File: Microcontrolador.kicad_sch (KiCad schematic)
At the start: 3 parts

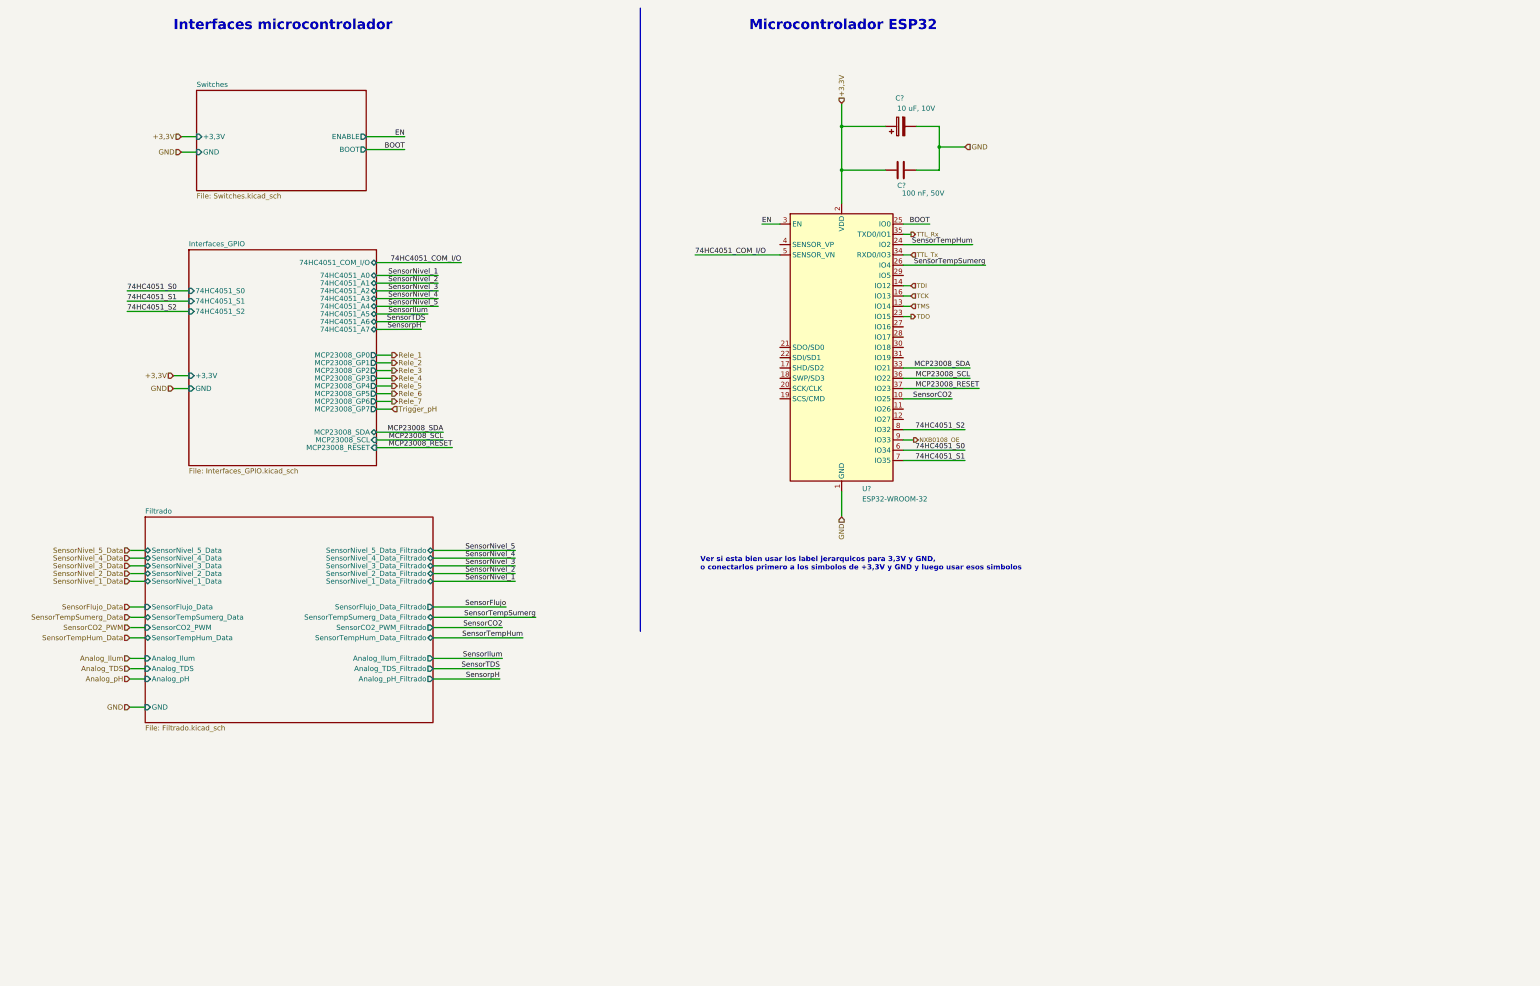
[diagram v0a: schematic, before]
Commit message: Ajuste del esquematico
Se cambio el integrado ESP32 por 2 tiras de pines de 1x15, se quitaron los switches EN y BOOT que ya estan en el NodeMCU, se quito el mutliplexor 74HC y se cablearon las I/O
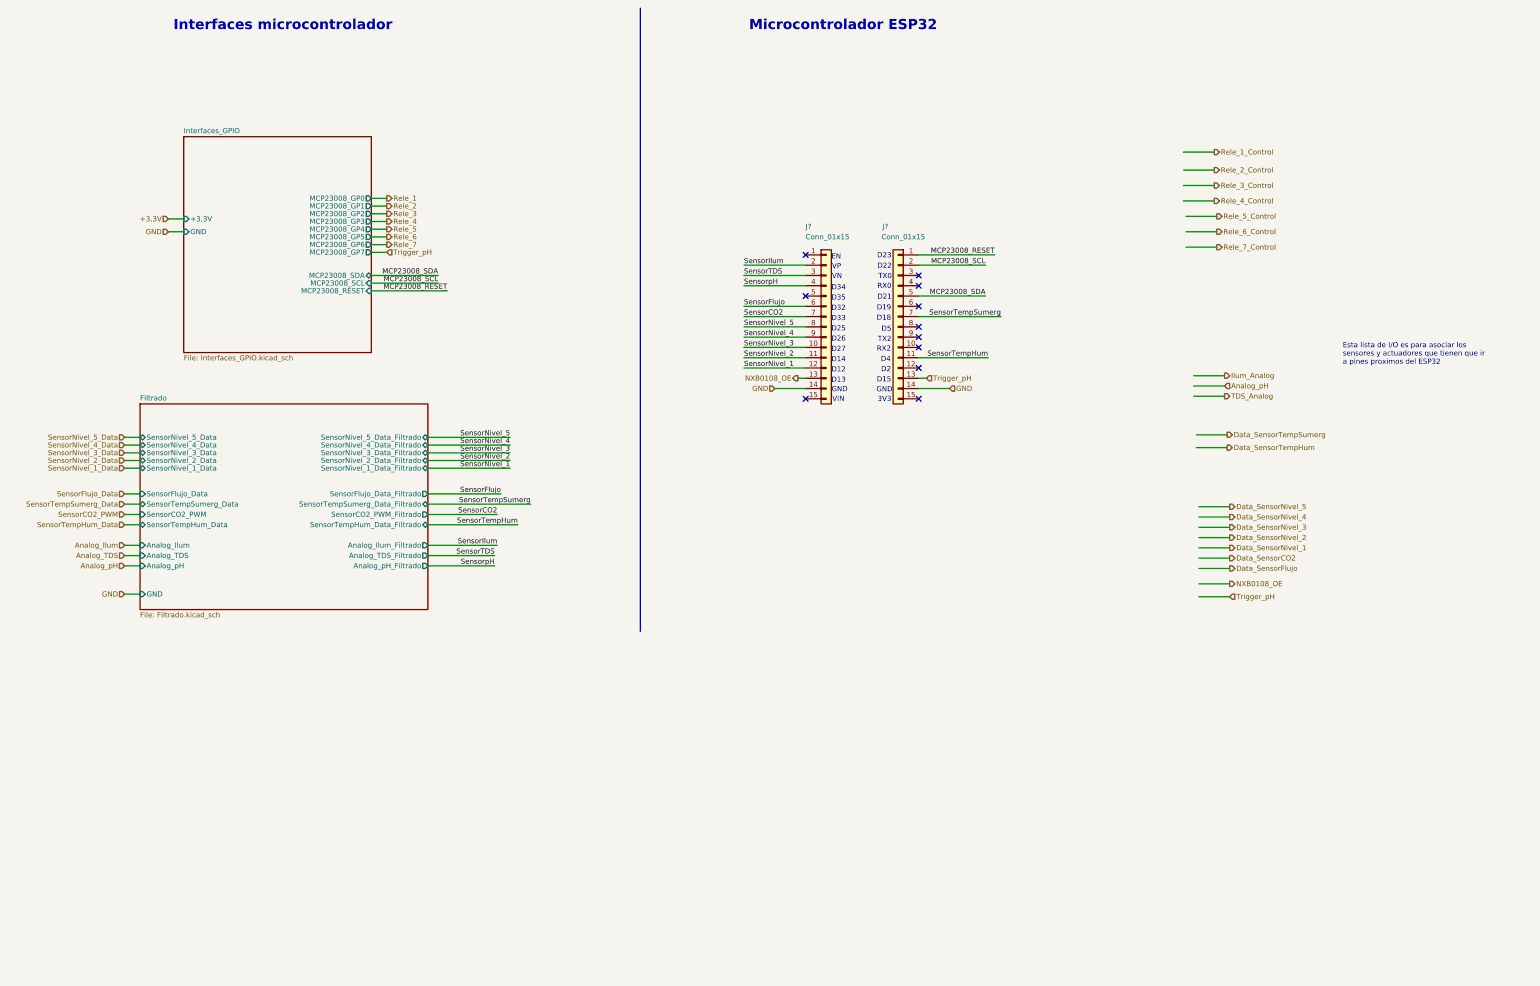
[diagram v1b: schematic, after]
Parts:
- removed C?: 100 nF, 50V, symbol Device:C
- removed C?: 10 uF, 10V, symbol Device:C_Polarized
- removed U?: ESP32-WROOM-32, RF_Module:ESP32-WROOM-32, symbol RF_Module:ESP32-WROOM-32
- added J?: Conn_01x15, symbol Connector_Generic:Conn_01x15
- added J?: Conn_01x15, Connector_JST:JST_SUR_SM08B-SURS-TF_1x08-1MP_P0.80mm_Horizontal, symbol Connector_Generic:Conn_01x15
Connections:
- net GND: now also J?.14 (Pin_14), J?.14 (Pin_14)
- net MCP23008_RESET: now also J?.1 (Pin_1)
- net MCP23008_SCL: now also J?.2 (Pin_2)
- net MCP23008_SDA: now also J?.5 (Pin_5)
- net NXB0108_OE: now also J?.13 (Pin_13)
- net SensorCO2: now also J?.7 (Pin_7)
- net SensorFlujo: now also J?.6 (Pin_6)
- net SensorIlum: now also J?.2 (Pin_2)
- net SensorNivel_1: now also J?.12 (Pin_12)
- net SensorNivel_2: now also J?.11 (Pin_11)
- net SensorNivel_3: now also J?.10 (Pin_10)
- net SensorNivel_4: now also J?.9 (Pin_9)
- net SensorNivel_5: now also J?.8 (Pin_8)
- net SensorTDS: now also J?.3 (Pin_3)
- net SensorTempHum: now also J?.11 (Pin_11)
- net SensorTempSumerg: now also J?.7 (Pin_7)
- net SensorpH: now also J?.4 (Pin_4)
- net Trigger_pH: now also J?.13 (Pin_13)
- no-connect marks 0 -> 11
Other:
- removed sheet Switches
- sheet Interfaces_GPIO ports: added none; removed 74HC4051_A0, 74HC4051_A1, 74HC4051_A2, 74HC4051_A3, 74HC4051_A4, 74HC4051_A5, 74HC4051_A6, 74HC4051_A7, 74HC4051_COM_I/O, 74HC4051_S0, 74HC4051_S1, 74HC4051_S2
- note added: "3V3"
- note added: "D12"
- note added: "D13"
- note added: "D14"
- note added: "D15"
- note added: "D18"
- note added: "D19"
- note added: "D2"
- note added: "D21"
- note added: "D22"
- note added: "D23"
- note added: "D25"
- note added: "D26"
- note added: "D27"
- note added: "D32"
- note added: "D33"
- note added: "D34"
- note added: "D35"
- note added: "D4"
- note added: "D5"
- note added: "EN"
- note added: "Esta lista de I/O es para asociar los sensores y actuadores que tienen que ir a pines proximos del ESP32"
- note added: "GND"
- note added: "RX0"
- note added: "RX2"
- note added: "TX0"
- note added: "TX2"
- note added: "VIN"
- note added: "VN"
- note added: "VP"
- note removed: "Ver si esta bien usar los label jerarquicos para 3,3V y GND, o conectarlos primero a los simbolos de +3,3V y GND y luego usar esos simbolos"

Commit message: Modificación de posición de circ. filtrado y circ. de adaptación de tensión
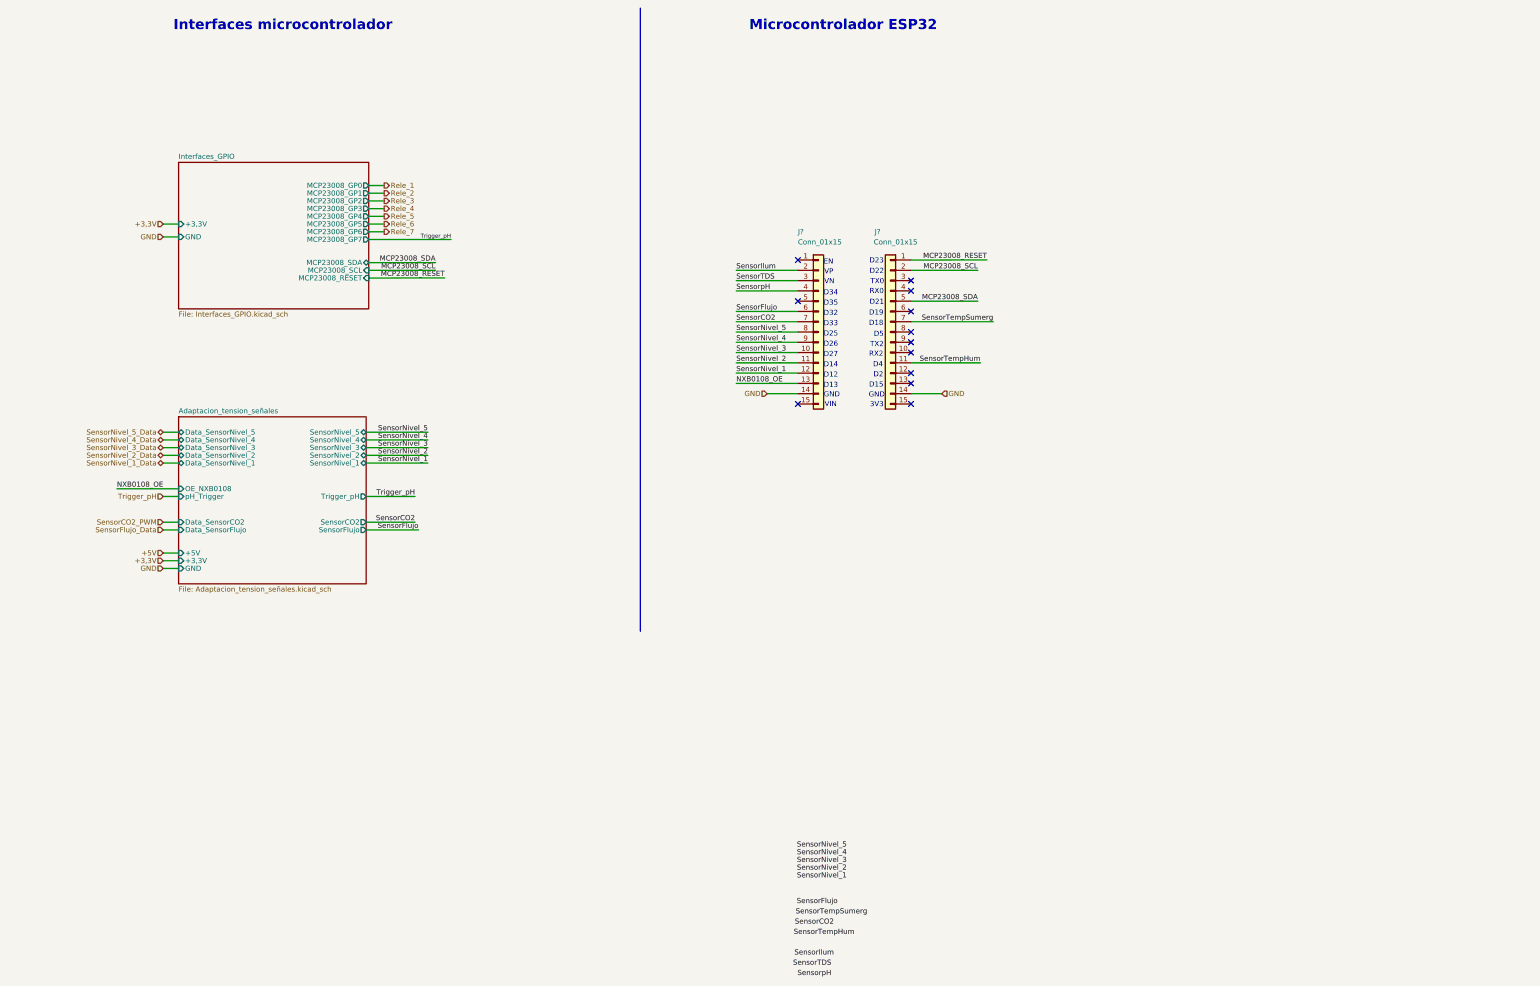
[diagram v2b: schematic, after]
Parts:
- removed J?: Conn_01x15, symbol Connector_Generic:Conn_01x15
- removed J?: Conn_01x15, Connector_JST:JST_SUR_SM08B-SURS-TF_1x08-1MP_P0.80mm_Horizontal, symbol Connector_Generic:Conn_01x15
- added J? (x2): Conn_01x15, Connector_JST:JST_SUR_SM08B-SURS-TF_1x08-1MP_P0.80mm_Horizontal, symbol Connector_Generic:Conn_01x15
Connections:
- net GND: now also J?.14 (Pin_14), J?.14 (Pin_14)
- net MCP23008_RESET: now also J?.1 (Pin_1)
- net MCP23008_SCL: now also J?.2 (Pin_2)
- net MCP23008_SDA: now also J?.5 (Pin_5)
- net NXB0108_OE: now also J?.13 (Pin_13)
- net SensorCO2: now also J?.7 (Pin_7)
- net SensorFlujo: now also J?.6 (Pin_6)
- net SensorIlum: now also J?.2 (Pin_2)
- net SensorNivel_1: now also J?.12 (Pin_12)
- net SensorNivel_2: now also J?.11 (Pin_11)
- net SensorNivel_3: now also J?.10 (Pin_10)
- net SensorNivel_4: now also J?.9 (Pin_9)
- net SensorNivel_5: now also J?.8 (Pin_8)
- net SensorTDS: now also J?.3 (Pin_3)
- net SensorTempHum: now also J?.11 (Pin_11)
- net SensorTempSumerg: now also J?.7 (Pin_7)
- net SensorpH: now also J?.4 (Pin_4)
- no-connect marks 11 -> 12
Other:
- removed sheet Filtrado
- added sheet Adaptacion_tension_señales (Adaptacion_tension_señales.kicad_sch)
- note removed: "Esta lista de I/O es para asociar los sensores y actuadores que tienen que ir a pines proximos del ESP32"

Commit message: Corrección de errores menores de esquematico
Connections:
- net SensorIlum: no longer J?.2 (Pin_2)
- net SensorTDS: no longer J?.3 (Pin_3)
- net SensorTempHum: no longer J?.11 (Pin_11)
- net SensorTempSumerg: no longer J?.7 (Pin_7)
- net SensorpH: no longer J?.4 (Pin_4)
- new net Analog_Ilum: J?.2 (Pin_2)
- new net Analog_TDS: J?.3 (Pin_3)
- new net Analog_pH: J?.4 (Pin_4)
- new net SensorTempHum_Data: J?.11 (Pin_11)
- new net SensorTempSumerg_Data: J?.7 (Pin_7)
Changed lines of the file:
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@@
+    (stroke (width 0) (type default) (color 0 0 0 0))
+  )
+  (wire (pts (xy 212.09 81.915) (xy 215.9 81.915))
     (stroke (width 0) (type default) (color 0 0 0 0))
   )
@@
     (stroke (width 0) (type default) (color 0 0 0 0))
   )
+  (wire (pts (xy 212.09 79.375) (xy 215.9 79.375))
+    (stroke (width 0) (type default) (color 0 0 0 0))
+  )
   (wire (pts (xy 109.855 69.215) (xy 130.175 69.215))
     (stroke (width 0) (type default) (color 0 0 0 0))
@@
     (stroke (width 0) (type default) (color 0 0 0 0))
   )
-  (wire (pts (xy 243.84 99.695) (xy 260.985 99.695))
-    (stroke (width 0) (type default) (color 0 0 0 0))
-  )
   (wire (pts (xy 109.22 118.745) (xy 124.46 118.745))
     (stroke (width 0) (type default) (color 0 0 0 0))
@@
     (stroke (width 0) (type default) (color 0 0 0 0))
   )
+  (wire (pts (xy 247.65 99.695) (xy 243.84 99.695))
+    (stroke (width 0) (type default) (color 0 0 0 0))
+  )
   (wire (pts (xy 59.055 146.685) (xy 62.865 146.685))
     (stroke (width 0) (type default) (color 0 0 0 0))
@@
     (stroke (width 0) (type default) (color 0 0 0 0))
   )
+  (wire (pts (xy 212.09 76.835) (xy 215.9 76.835))
+    (stroke (width 0) (type default) (color 0 0 0 0))
+  )
   (wire (pts (xy 113.665 67.31) (xy 109.855 67.31))
     (stroke (width 0) (type default) (color 0 0 0 0))
@@
     (stroke (width 0) (type default) (color 0 0 0 0))
   )
-  (wire (pts (xy 200.66 79.375) (xy 215.9 79.375))
-    (stroke (width 0) (type default) (color 0 0 0 0))
-  )
   (wire (pts (xy 59.055 122.555) (xy 62.865 122.555))
     (stroke (width 0) (type default) (color 0 0 0 0))
@@
     (stroke (width 0) (type default) (color 0 0 0 0))
   )
-  (wire (pts (xy 243.84 89.535) (xy 264.16 89.535))
-    (stroke (width 0) (type default) (color 0 0 0 0))
-  )
   (wire (pts (xy 59.055 68.58) (xy 62.865 68.58))
     (stroke (width 0) (type default) (color 0 0 0 0))
@@
     (stroke (width 0) (type default) (color 0 0 0 0))
   )
-  (wire (pts (xy 200.66 76.835) (xy 215.9 76.835))
+  (wire (pts (xy 247.65 89.535) (xy 243.84 89.535))
     (stroke (width 0) (type default) (color 0 0 0 0))
   )
@@
   )
   (wire (pts (xy 215.9 99.695) (xy 200.66 99.695))
-    (stroke (width 0) (type default) (color 0 0 0 0))
-  )
-  (wire (pts (xy 200.66 81.915) (xy 215.9 81.915))
     (stroke (width 0) (type default) (color 0 0 0 0))
   )
@@
     (effects (font (size 1.27 1.27)) (justify right bottom))
   )
-  (label "SensorTempSumerg" (at 264.16 89.535 180)
-    (effects (font (size 1.27 1.27)) (justify right bottom))
-  )
   (label "SensorNivel_2" (at 200.66 99.695 0)
     (effects (font (size 1.27 1.27)) (justify left bottom))
@@
     (effects (font (size 1.27 1.27)) (justify right bottom))
   )
-  (label "SensorTempHum" (at 260.985 99.695 180)
-    (effects (font (size 1.27 1.27)) (justify right bottom))
-  )
   (label "SensorFlujo" (at 200.66 86.995 0)
     (effects (font (size 1.27 1.27)) (justify left bottom))
@@
   )
   (label "NXB0108_OE" (at 200.66 104.775 0)
-    (effects (font (size 1.27 1.27)) (justify left bottom))
-  )
-  (label "SensorpH" (at 200.66 81.915 0)
-    (effects (font (size 1.27 1.27)) (justify left bottom))
-  )
-  (label "SensorTDS" (at 200.66 79.375 0)
     (effects (font (size 1.27 1.27)) (justify left bottom))
   )
@@
     (effects (font (size 1.27 1.27)) (justify left bottom))
   )
-  (label "SensorIlum" (at 200.66 76.835 0)
-    (effects (font (size 1.27 1.27)) (justify left bottom))
-  )
   (label "SensorCO2" (at 224.79 238.76 180)
     (effects (font (size 1.27 1.27)) (justify right bottom))
@@
     (effects (font (size 1.27 1.27)) (justify right bottom))
   )
+  (hierarchical_label "SensorTempHum_Data" (shape bidirectional) (at 247.65 99.695 0)
+    (effects (font (size 1.27 1.27)) (justify left))
+  )
   (hierarchical_label "+5V" (shape input) (at 59.055 146.685 180)
     (effects (font (size 1.27 1.27)) (justify right))
@@
     (effects (font (size 1.27 1.27)) (justify right))
   )
+  (hierarchical_label "Analog_TDS" (shape input) (at 212.09 79.375 180)
+    (effects (font (size 1.27 1.27)) (justify right))
+  )
   (hierarchical_label "GND" (shape input) (at 208.28 107.315 180)
     (effects (font (size 1.27 1.27)) (justify right))
@@
     (effects (font (size 1.27 1.27)) (justify left))
   )
+  (hierarchical_label "Analog_Ilum" (shape input) (at 212.09 76.835 180)
+    (effects (font (size 1.27 1.27)) (justify right))
+  )
   (hierarchical_label "SensorNivel_2_Data" (shape bidirectional) (at 59.055 122.555 180)
     (effects (font (size 1.27 1.27)) (justify right))
@@
     (effects (font (size 1.27 1.27)) (justify right))
   )
+  (hierarchical_label "SensorTempSumerg_Data" (shape bidirectional) (at 247.65 89.535 0)
+    (effects (font (size 1.27 1.27)) (justify left))
+  )
   (hierarchical_label "GND" (shape input) (at 59.055 150.495 180)
     (effects (font (size 1.27 1.27)) (justify right))
@@
     (effects (font (size 1.27 1.27)) (justify left))
   )
+  (hierarchical_label "Analog_pH" (shape input) (at 212.09 81.915 180)
+    (effects (font (size 1.27 1.27)) (justify right))
+  )
   (hierarchical_label "Rele_2" (shape output) (at 113.665 57.785 0)
